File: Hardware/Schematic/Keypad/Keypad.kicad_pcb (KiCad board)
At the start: 2 copper layers, 9 parts, among them J9 Conn_01x02, U1 TCA8418RTWR

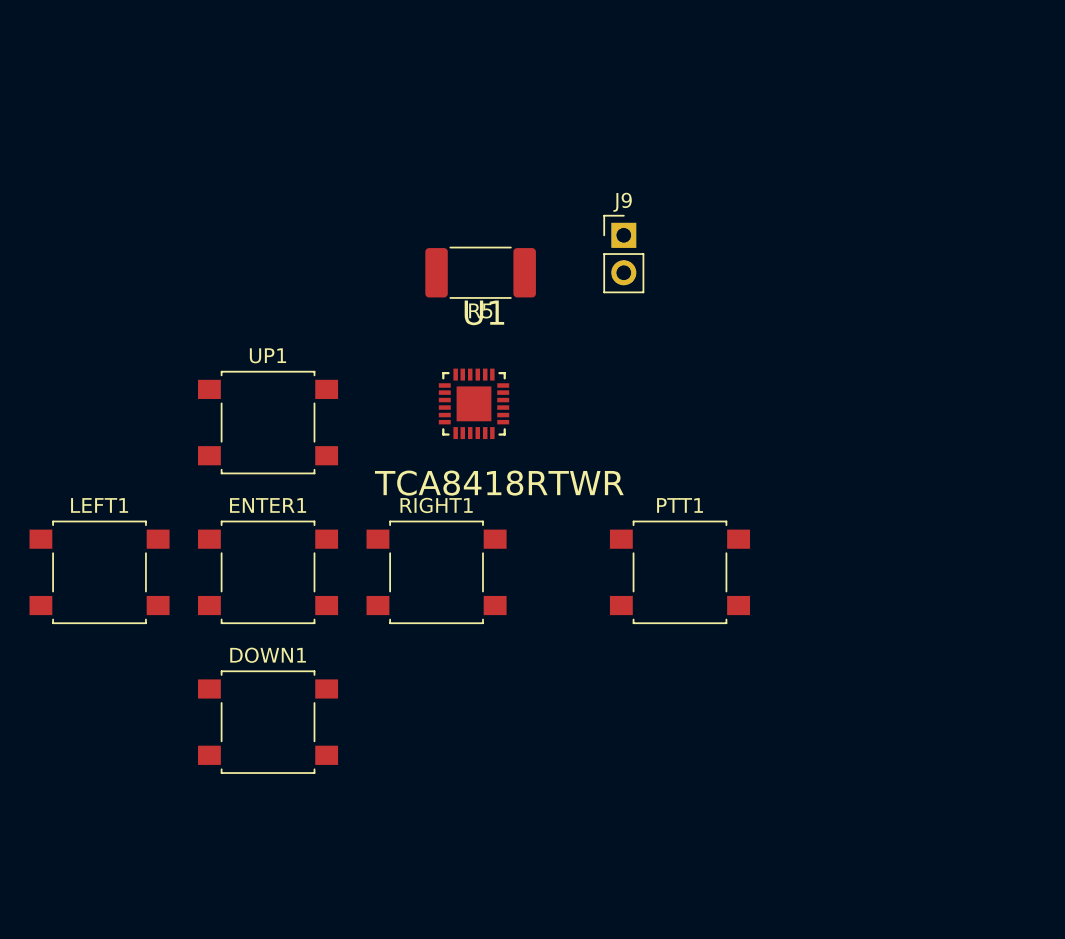
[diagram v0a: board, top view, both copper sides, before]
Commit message: Updated keypad and display schematic to use header sockets for intra-board connections.
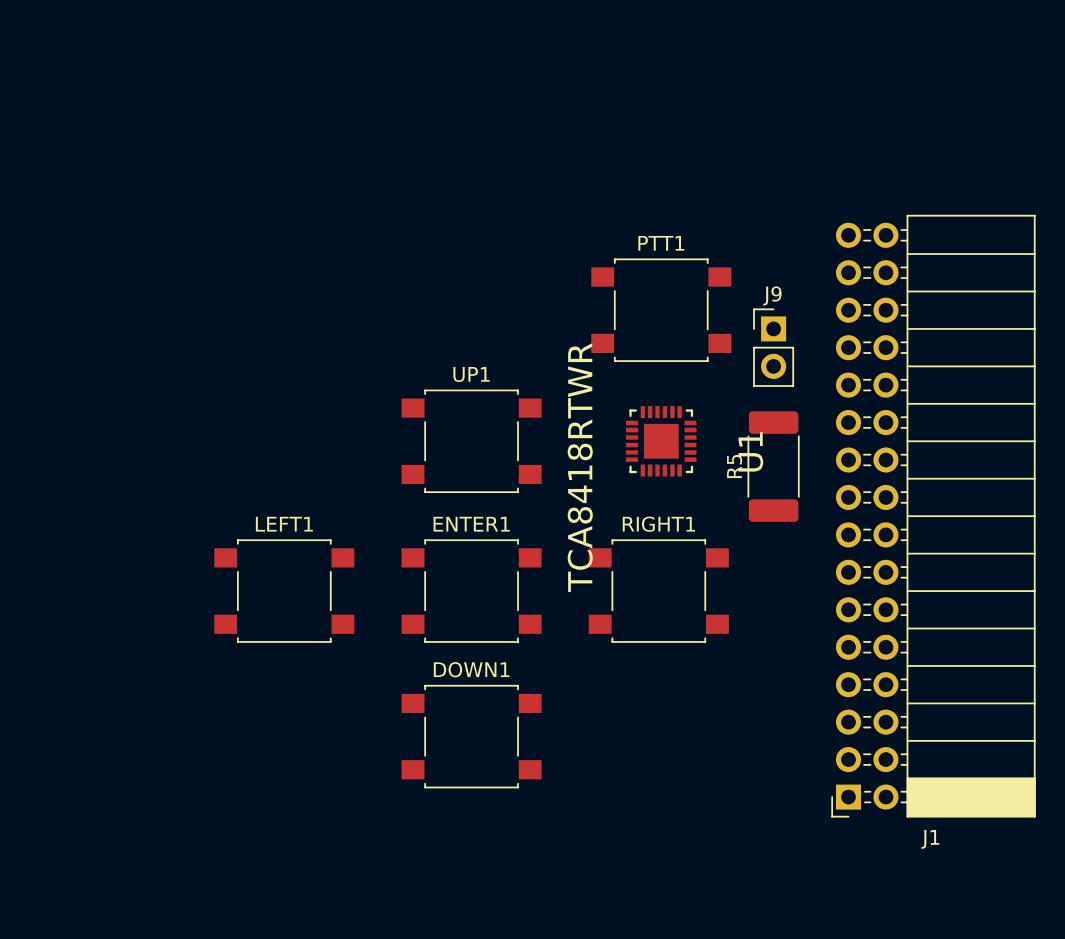
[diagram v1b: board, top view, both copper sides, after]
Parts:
- added J1: Conn_01x32, Connector_PinSocket_2.54mm:PinSocket_2x16_P2.54mm_Horizontal, F.Cu at (175.3, 125.7)
- moved R5 23.8 mm to (170.2, 103.3), turned to 90 degrees
- moved PTT1 17.8 mm to (162.6, 92.7)
- moved RIGHT1 15.1 mm to (162.4, 111.8)
- moved ENTER1 13.9 mm to (149.7, 111.8)
- moved UP1 13.9 mm to (149.7, 101.6)
- moved DOWN1 13.8 mm to (149.7, 121.6)
- moved U1 13.0 mm to (162.6, 101.6), turned to 270 degrees
- moved LEFT1 12.6 mm to (137.0, 111.8)
- moved J9 12.0 mm to (170.2, 94.0)

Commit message: Added male 02x16 header to auxillary boards so they can be "stacked" together
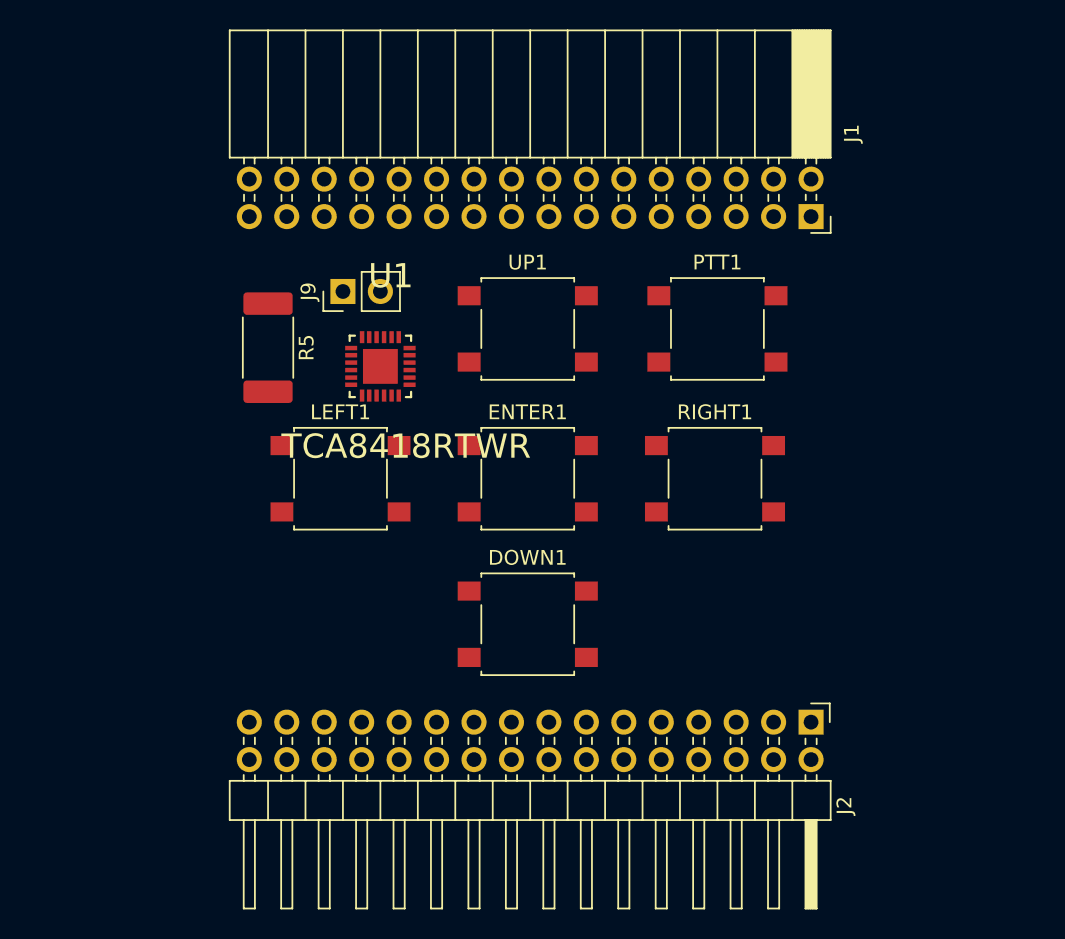
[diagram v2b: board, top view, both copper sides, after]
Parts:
- added J2: Conn_01x32, Connector_PinHeader_2.54mm:PinHeader_2x16_P2.54mm_Horizontal, F.Cu at (172.7, 120.7)
- moved J1 39.5 mm to (172.7, 86.4), turned to 270 degrees
- moved R5 35.2 mm to (135.9, 95.2), turned to 270 degrees
- moved J9 29.3 mm to (141.0, 91.4), turned to 90 degrees
- moved U1 19.7 mm to (143.5, 96.5), turned to 0 degrees
- moved ENTER1 8.52 mm to (153.5, 104.1)
- moved LEFT1 8.52 mm to (140.8, 104.1)
- moved RIGHT1 8.52 mm to (166.2, 104.1)
- moved DOWN1 8.52 mm to (153.5, 114.0)
- moved UP1 8.52 mm to (153.5, 94.0)
- moved PTT1 4.02 mm to (166.4, 94.0)
